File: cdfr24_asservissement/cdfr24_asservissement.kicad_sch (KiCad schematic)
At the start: 55 parts, among them J1 Connecteur batterie, J10 Free Connecteur, J11 Conn_01x02, J12 Conn_01x02, J13 Connecteur Odométrie, J14 Conn_ST_STDC14, J2 Conn_01x03, J3 Conn_01x05, J5 Conn_01x03, J6 Connecteur Odométrie, J7 Conn_01x03, Q1 Q_NMOS_GDS, U2 TVN 5-2411WI, U3 STM32F401RCTx, U4 LD1117S33TR_SOT223

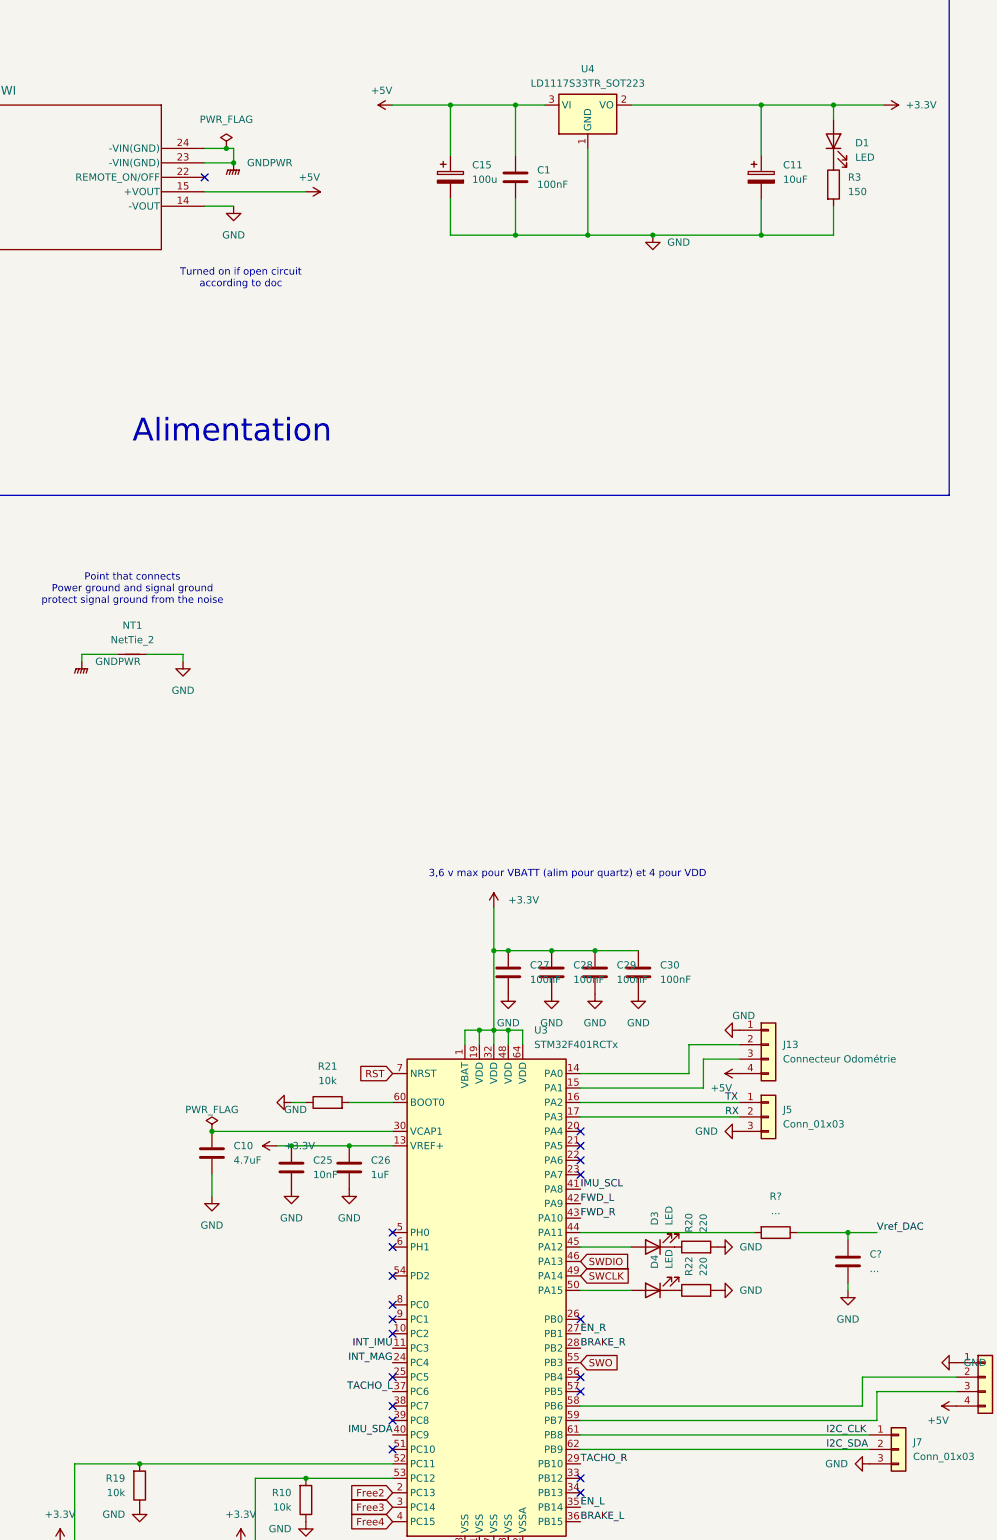
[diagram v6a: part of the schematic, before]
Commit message: Add LEDs and remove capacitor
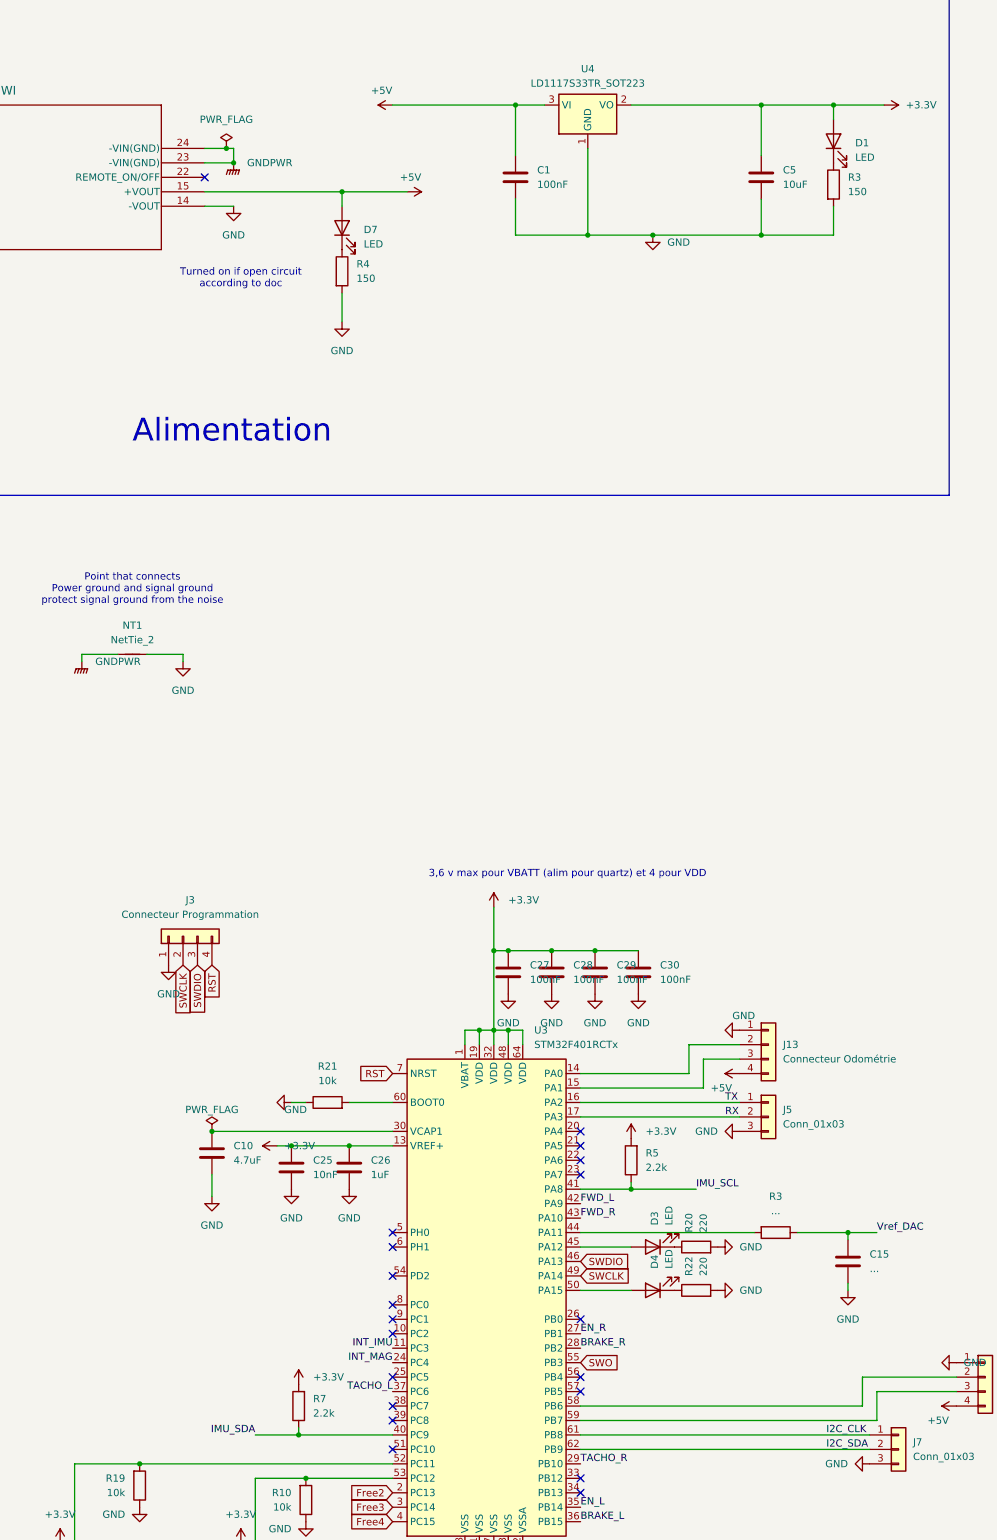
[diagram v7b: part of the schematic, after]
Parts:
- removed C11: 10uF, Capacitor_SMD:CP_Elec_10x10.5, symbol Device:C_Polarized
- removed C15: 100u, Capacitor_SMD:CP_Elec_10x10.5, symbol Device:C_Polarized
- added C5: 10uF, symbol Device:C
- added D7: LED, LED_SMD:LED_0805_2012Metric_Pad1.15x1.40mm_HandSolder, symbol Device:LED
- added J3: Connecteur Programmation, Connector_PinHeader_2.54mm:PinHeader_1x04_P2.54mm_Vertical, symbol Connector_Generic:Conn_01x04
- added R4: 150, Resistor_SMD:R_0805_2012Metric_Pad1.20x1.40mm_HandSolder, symbol Device:R
- added R5, R7: 2.2k, Resistor_SMD:R_0805_2012Metric_Pad1.20x1.40mm_HandSolder, symbol Device:R
- gave numbers to parts that had none: 2
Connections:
- net +3.3V: now also C5.1, R5.2, R7.2
- net +5V: now also D7.2 (A)
- net GND: now also C5.2, J3.1 (Pin_1), R4.2
- net IMU_SCL: now also R5.1
- net IMU_SDA: now also R7.1
- net RST: now also J3.4 (Pin_4)
- net SWCLK: now also J3.2 (Pin_2)
- net SWDIO: now also J3.3 (Pin_3)
- new net: D7.1 (K), R4.1

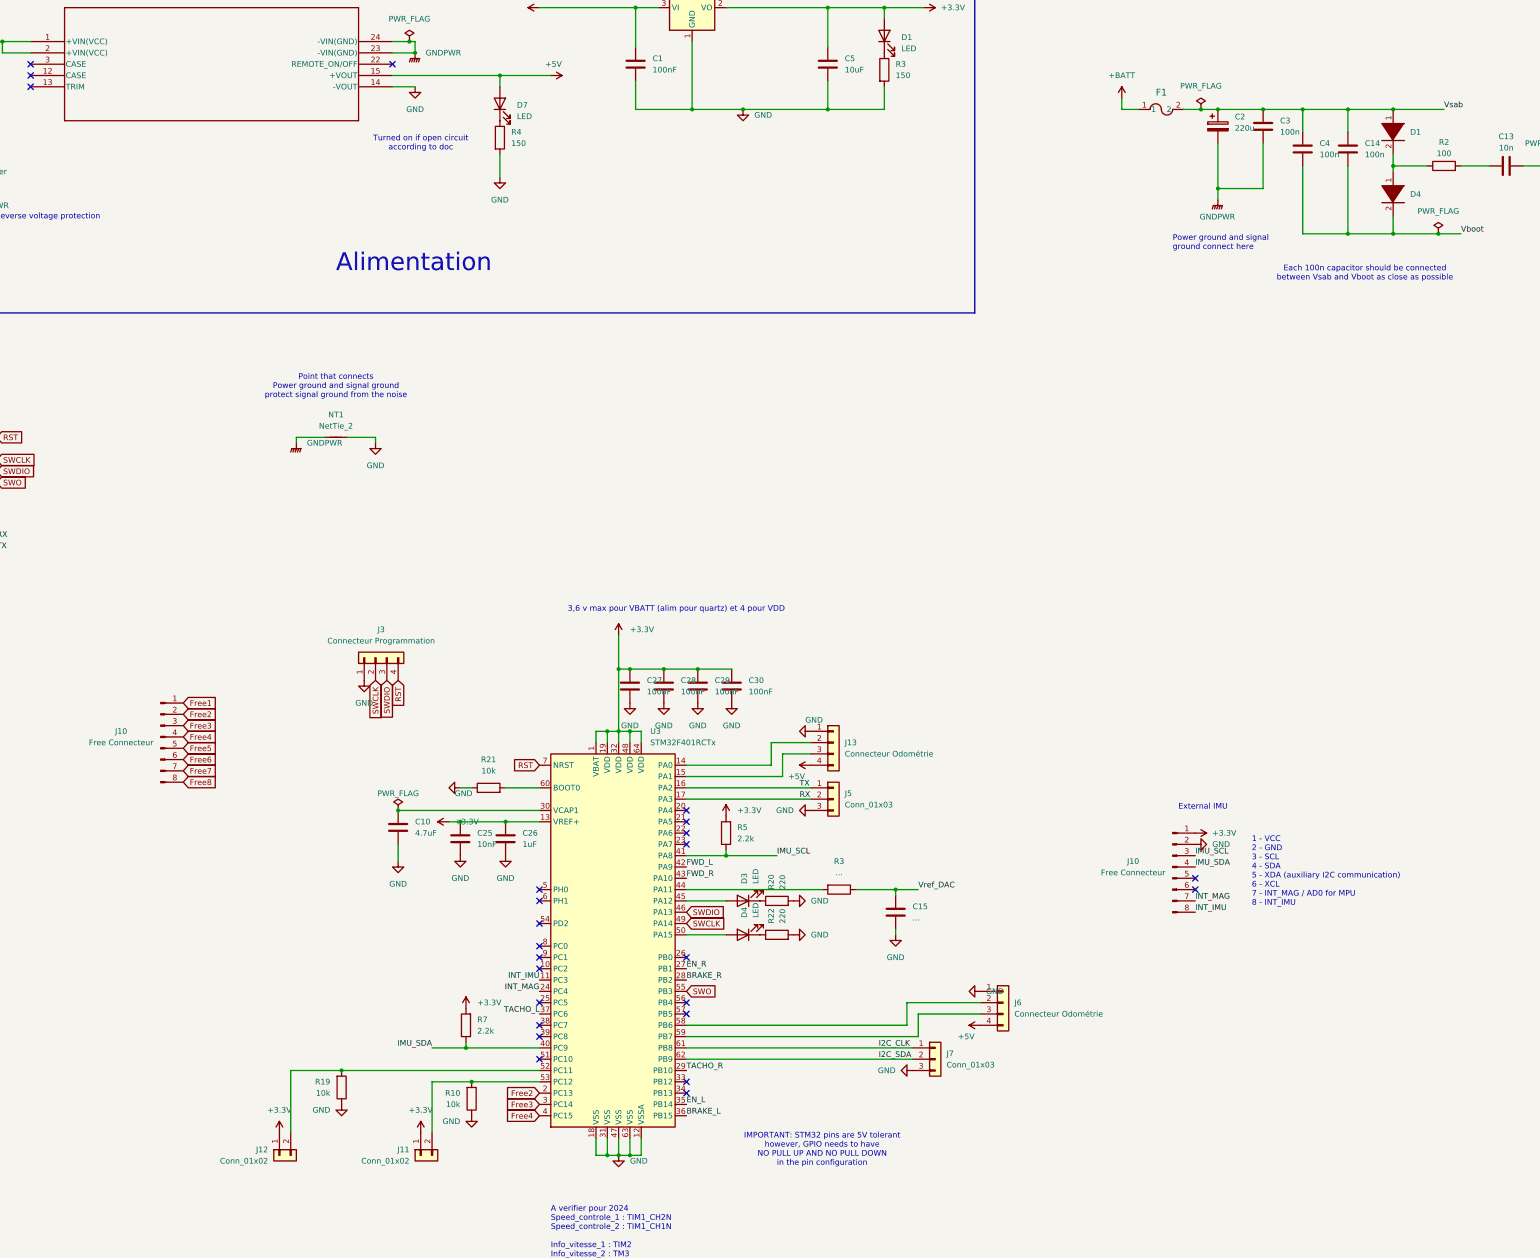
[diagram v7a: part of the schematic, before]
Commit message: Fix warnings, add DIP switches
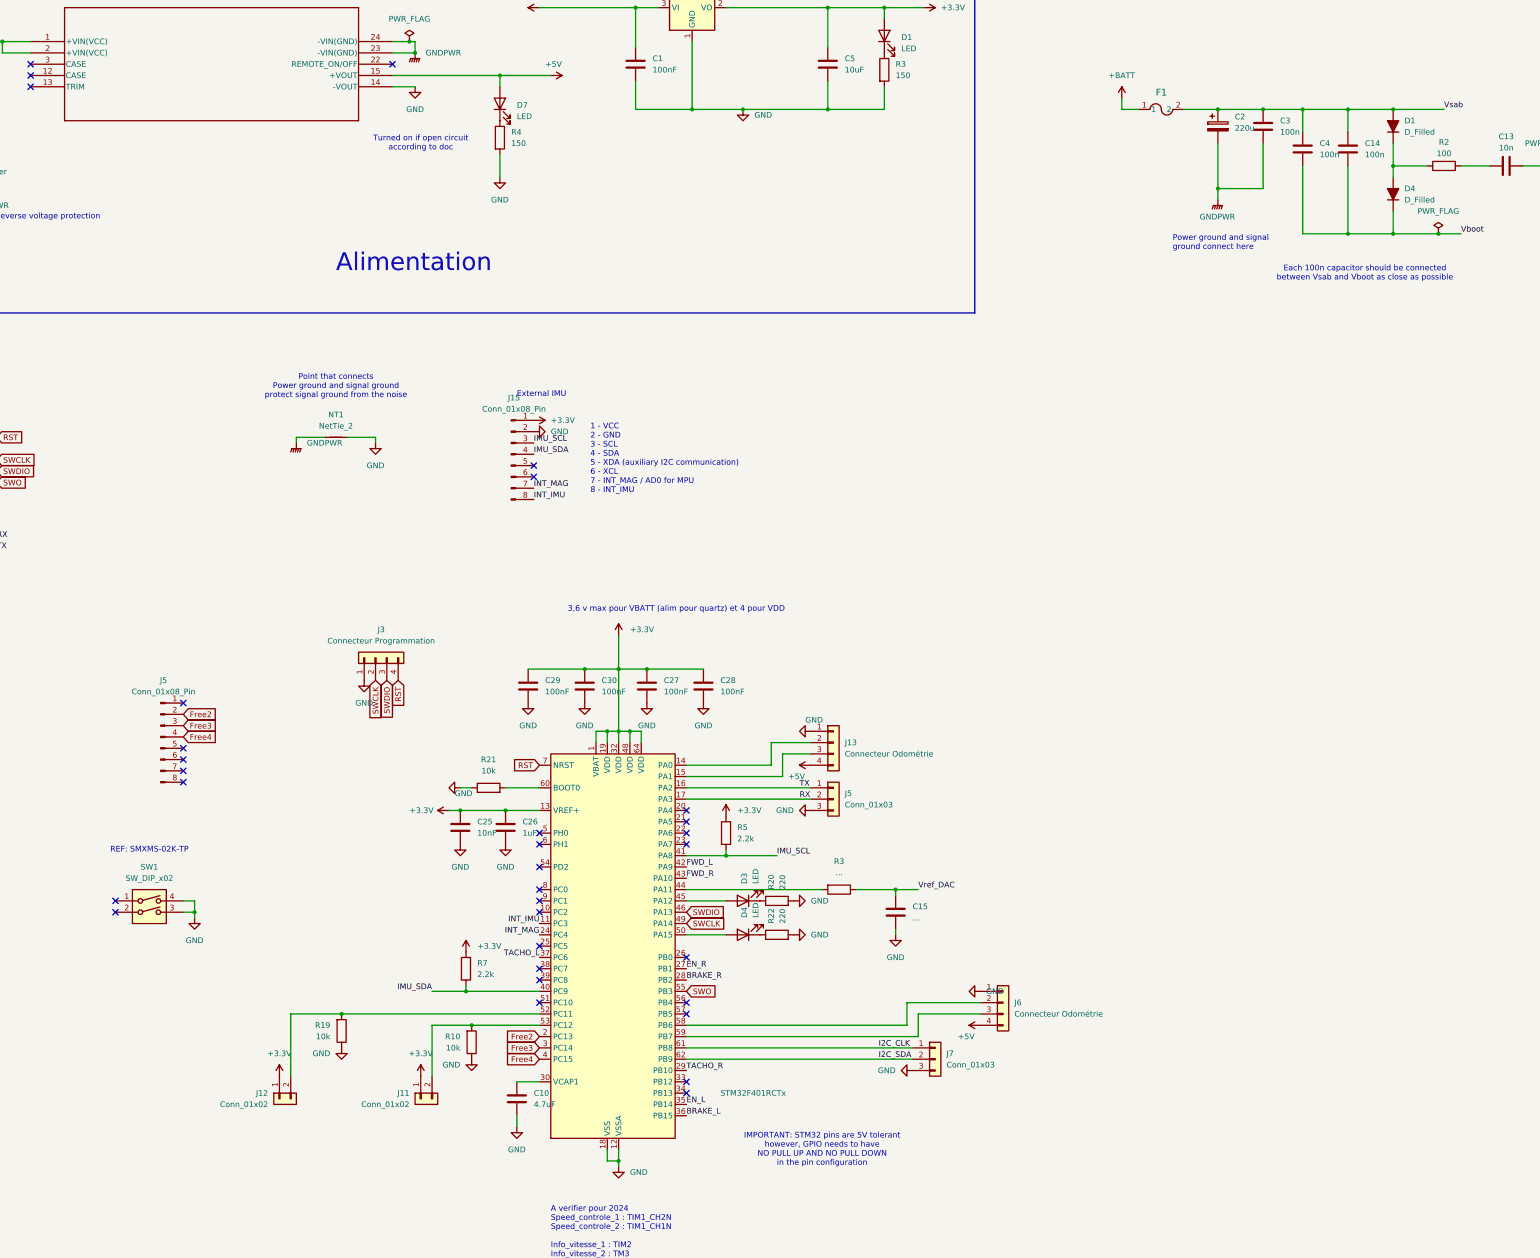
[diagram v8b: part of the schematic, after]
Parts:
- removed D1, D4: DIODE, B170B:DIOM505270X240, symbol pspice:DIODE
- removed J10 (x2): Free Connecteur, Connector_PinHeader_2.54mm:PinHeader_1x08_P2.54mm_Vertical, symbol Connector:Conn_01x08_Male
- removed U3: STM32F401RCTx, Package_QFP:LQFP-64_10x10mm_P0.5mm, symbol MCU_ST_STM32F4:STM32F401RCTx
- added D1, D4: D_Filled, B170B:DIOM505270X240, symbol Device:D_Filled
- added J15, J5: Conn_01x08_Pin, Connector_PinHeader_2.54mm:PinHeader_1x08_P2.54mm_Vertical, symbol Connector:Conn_01x08_Pin
- added SW1: SW_DIP_x02, Button_Switch_SMD:SW_DIP_SPSTx02_Slide_Copal_CHS-02B_W7.62mm_P1.27mm, symbol Switch:SW_DIP_x02
- added U1: STM32F401RCTx, Package_QFP:LQFP-64_10x10mm_P0.5mm, symbol MCU_ST_STM32F4:STM32F401RCTx
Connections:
- net +3.3V: now also J15.1 (Pin_1), U1.1 (VBAT), U1.13 (VREF+), U1.19 (VDD), U1.32 (VDD), U1.48 (VDD), U1.64 (VDD)
- net BRAKE_L: now also U1.36 (PB15)
- net BRAKE_R: now also U1.28 (PB2)
- net EN_L: now also U1.35 (PB14)
- net EN_R: now also U1.27 (PB1)
- net FWD_L: now also U1.42 (PA9)
- net FWD_R: now also U1.43 (PA10)
- net Free2: now also J5.2 (Pin_2), U1.2 (PC13)
- net Free3: now also J5.3 (Pin_3), U1.3 (PC14)
- net Free4: now also J5.4 (Pin_4), U1.4 (PC15)
- net GND: now also J15.2 (Pin_2), SW1.3, SW1.4, U1.12 (VSSA), U1.18 (VSS), U1.31 (VSS), U1.47 (VSS), U1.63 (VSS)
- net I2C_CLK: now also U1.61 (PB8)
- net I2C_SDA: now also U1.62 (PB9)
- net IMU_SCL: now also J15.3 (Pin_3), U1.41 (PA8)
- net IMU_SDA: now also J15.4 (Pin_4), U1.40 (PC9)
- net INT_IMU: now also J15.8 (Pin_8), U1.11 (PC3)
- net INT_MAG: now also J15.7 (Pin_7), U1.24 (PC4)
- net RST: now also U1.7 (NRST)
- net RX: now also U1.17 (PA3)
- net SWCLK: now also U1.49 (PA14)
- net SWDIO: now also U1.46 (PA13)
- net SWO: now also U1.55 (PB3)
- net TACHO_L: now also U1.37 (PC6)
- net TACHO_R: now also U1.29 (PB10)
- net TX: now also U1.16 (PA2)
- net Vboot: now also D4.1 (K)
- net Vsab: now also D1.2 (A)
- net at J13.2 (Pin_2): now also U1.14 (PA0)
- net at J13.3 (Pin_3): now also U1.15 (PA1)
- net at J6.2 (Pin_2): now also U1.58 (PB6)
- net at J6.3 (Pin_3): now also U1.59 (PB7)
- net at D4.2 (A): now also U1.50 (PA15)
- net at R2.1: now also D1.1 (K), D4.2 (A)
- net at D3.2 (A): now also U1.45 (PA12)
- net at J12.2 (Pin_2), R19.2: now also U1.52 (PC11)
- net at R21.2: now also U1.60 (BOOT0)
- net at R3.2: now also U1.44 (PA11)
- net at C10.1: now also U1.30 (VCAP1)
- net at J11.2 (Pin_2), R10.2: now also U1.53 (PC12)
- no-connect marks 29 -> 36
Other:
- note added: "REF: SMXMS-02K-TP"
- moved on the sheet: C10, C25, C26, C27, C28, C29, C30, J11, J12, R10, R19, R7
